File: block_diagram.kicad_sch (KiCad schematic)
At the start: 0 parts

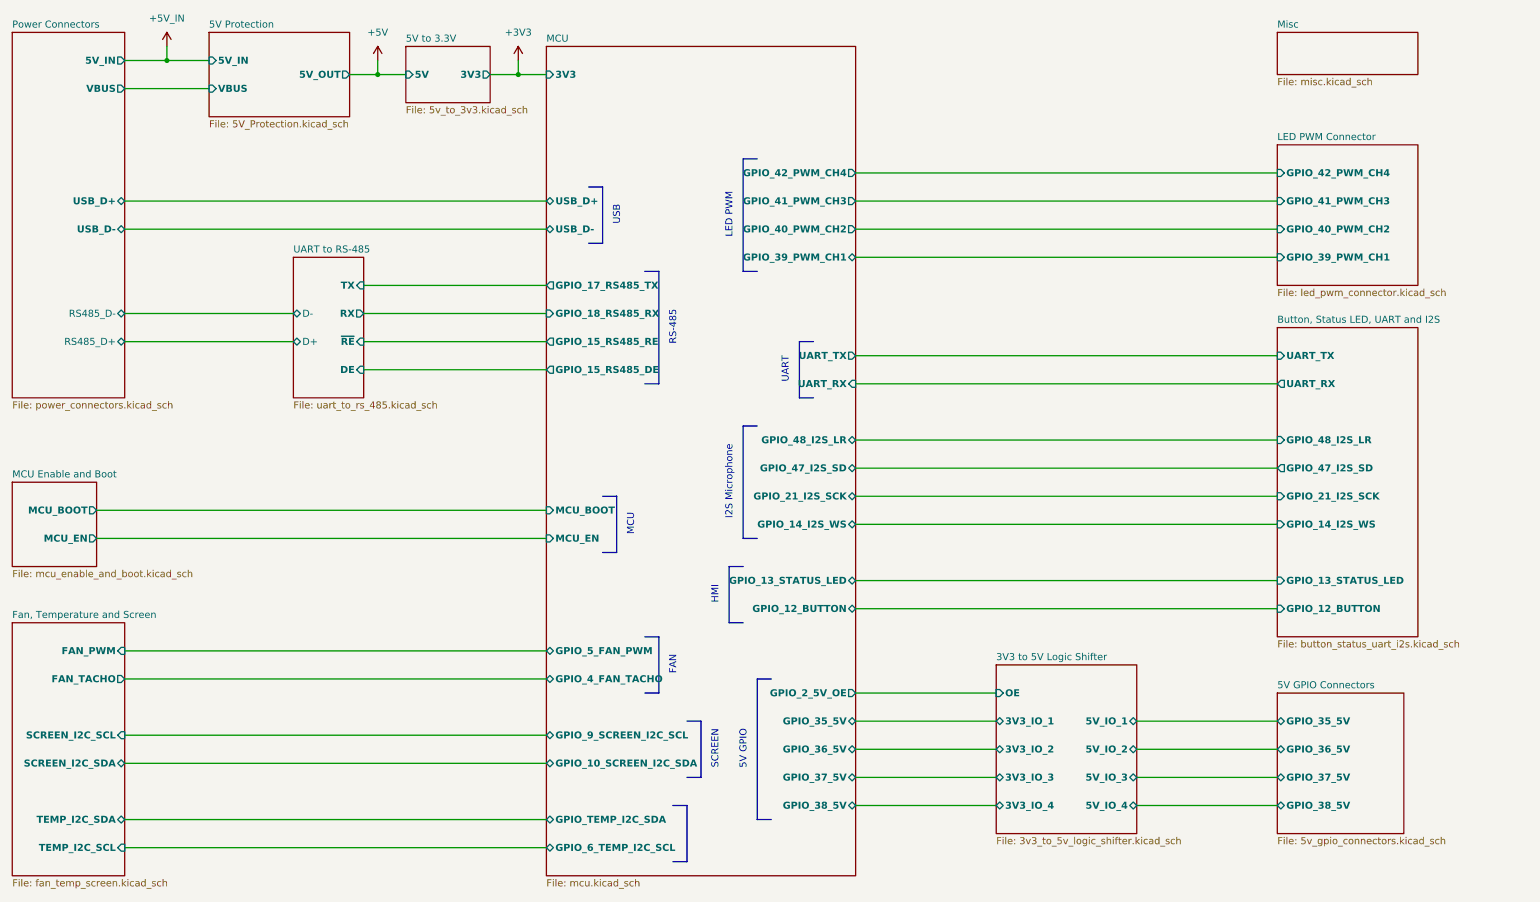
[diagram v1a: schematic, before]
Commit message: Finished layout no drc or erc errors
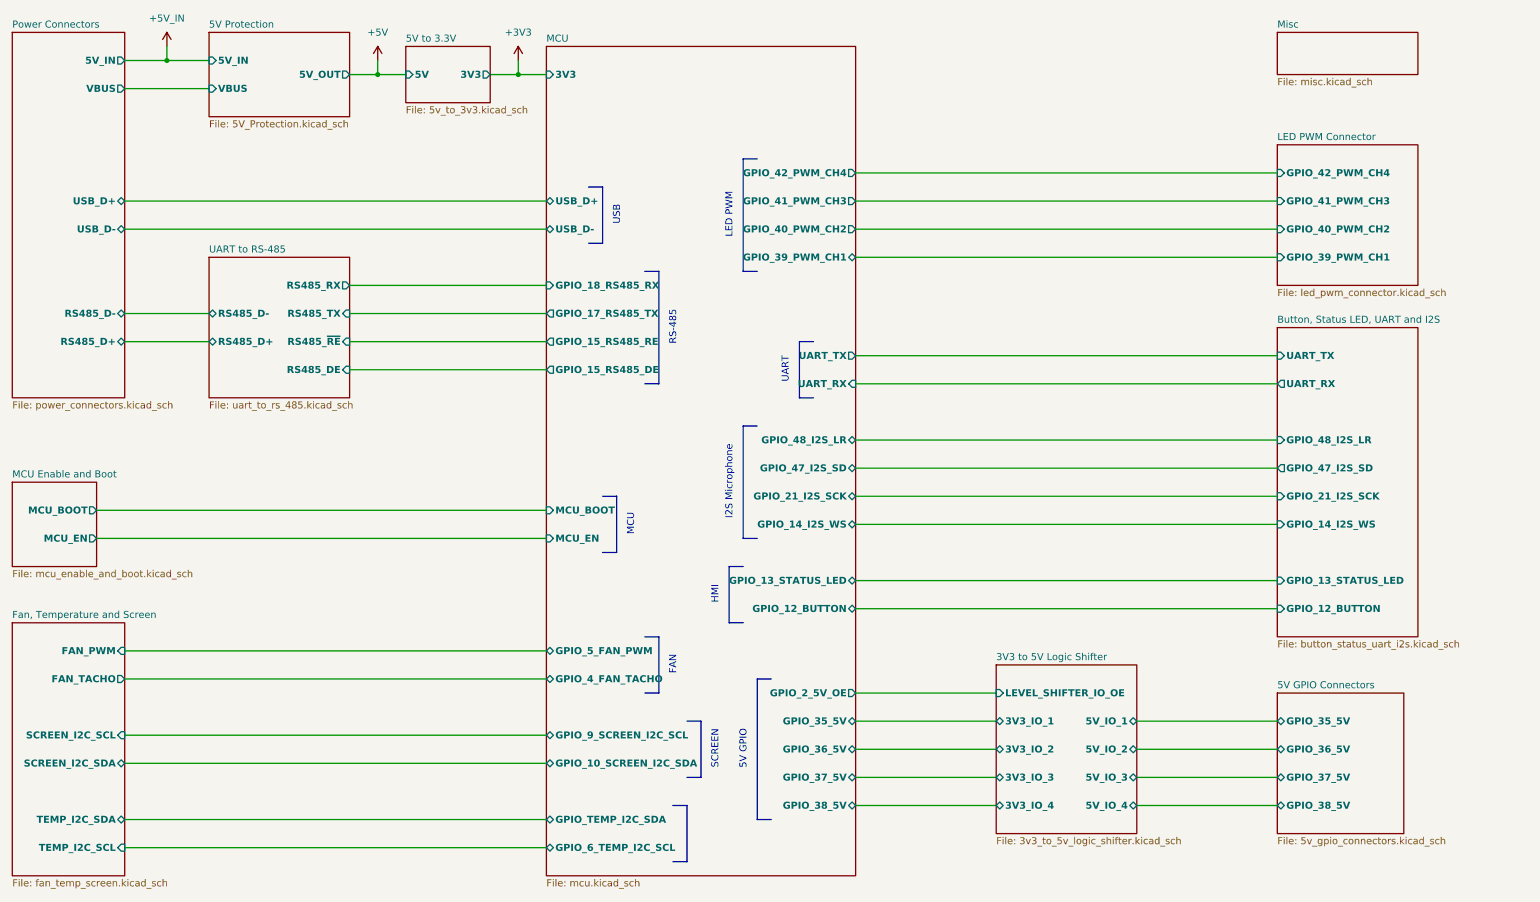
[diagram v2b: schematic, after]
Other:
- sheet 3V3 to 5V Logic Shifter ports: added LEVEL_SHIFTER_IO_OE; removed OE
- sheet UART to RS-485 ports: added RS485_D+, RS485_D-, RS485_DE, RS485_RX, RS485_TX, RS485_~{RE}; removed D+, D-, DE, RX, TX, ~{RE}
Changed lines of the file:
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@@
-	(wire
-		(pts
-			(xy 78.74 63.5) (xy 111.76 63.5)
-		)
-		(stroke
-			(width 0)
-			(type default)
-		)
-	)
 	(wire
 		(pts
@@
 		)
 	)
-	(wire
-		(pts
-			(xy 78.74 68.58) (xy 111.76 68.58)
-		)
-		(stroke
-			(width 0)
-			(type default)
-		)
-	)
 	(polyline
 		(pts
@@
 	(wire
 		(pts
+			(xy 76.2 78.74) (xy 111.76 78.74)
+		)
+		(stroke
+			(width 0)
+			(type default)
+		)
+	)
+	(wire
+		(pts
 			(xy 35.56 48.26) (xy 111.76 48.26)
 		)
@@
 		)
 	)
+	(wire
+		(pts
+			(xy 76.2 68.58) (xy 111.76 68.58)
+		)
+		(stroke
+			(width 0)
+			(type default)
+		)
+	)
 	(polyline
 		(pts
@@
 		)
 	)
+	(wire
+		(pts
+			(xy 76.2 63.5) (xy 111.76 63.5)
+		)
+		(stroke
+			(width 0)
+			(type default)
+		)
+	)
 	(polyline
 		(pts
@@
 		)
 	)
-	(wire
-		(pts
-			(xy 78.74 73.66) (xy 111.76 73.66)
-		)
-		(stroke
-			(width 0)
-			(type default)
-		)
-	)
 	(polyline
 		(pts
@@
 	(wire
 		(pts
-			(xy 35.56 68.58) (xy 66.04 68.58)
+			(xy 35.56 68.58) (xy 50.8 68.58)
 		)
 		(stroke
@@
 	(wire
 		(pts
-			(xy 35.56 73.66) (xy 66.04 73.66)
+			(xy 76.2 73.66) (xy 111.76 73.66)
+		)
+		(stroke
+			(width 0)
+			(type default)
+		)
+	)
+	(wire
+		(pts
+			(xy 35.56 73.66) (xy 50.8 73.66)
 		)
 		(stroke
@@
 		(pts
 			(xy 147.32 88.9) (xy 147.32 109.22)
-		)
-		(stroke
-			(width 0)
-			(type default)
-		)
-	)
-	(wire
-		(pts
-			(xy 78.74 78.74) (xy 111.76 78.74)
 		)
 		(stroke
@@
 			)
 		)
-		(pin "OE" input
-			(at 193.04 137.16 180)
-			(effects
-				(font
-					(size 1.27 1.27)
-					(thickness 0.254)
-					(bold yes)
-				)
-				(justify left)
-			)
-		)
 		(pin "3V3_IO_1" bidirectional
 			(at 193.04 142.24 180)
@@
 				)
 				(justify right)
+			)
+		)
+		(pin "LEVEL_SHIFTER_IO_OE" input
+			(at 193.04 137.16 180)
+			(effects
+				(font
+					(size 1.27 1.27)
+					(thickness 0.254)
+					(bold yes)
+				)
+				(justify left)
 			)
 		)
@@
 		)
 		(pin "GPIO_17_RS485_TX" output
+			(at 111.76 68.58 180)
+			(effects
+				(font
+					(size 1.27 1.27)
+					(thickness 0.254)
+					(bold yes)
+				)
+				(justify left)
+			)
+		)
+		(pin "GPIO_18_RS485_RX" input
 			(at 111.76 63.5 180)
-			(effects
-				(font
-					(size 1.27 1.27)
-					(thickness 0.254)
-					(bold yes)
-				)
-				(justify left)
-			)
-		)
-		(pin "GPIO_18_RS485_RX" input
-			(at 111.76 68.58 180)
 			(effects
 				(font
@@
 	)
 	(sheet
-		(at 66.04 58.42)
-		(size 12.7 25.4)
+		(at 50.8 58.42)
+		(size 25.4 25.4)
 		(fields_autoplaced yes)
 		(stroke
@@
 		)
 		(property "Sheetname" "UART to RS-485"
-			(at 66.04 57.7084 0)
+			(at 50.8 57.7084 0)
 			(effects
 				(font
@@
 		)
 		(property "Sheetfile" "uart_to_rs_485.kicad_sch"
-			(at 66.04 84.4046 0)
+			(at 50.8 84.4046 0)
 			(effects
 				(font
@@
 			)
 		)
-		(pin "DE" input
-			(at 78.74 78.74 0)
-			(effects
-				(font
-					(size 1.27 1.27)
-					(thickness 0.254)
-					(bold yes)
-				)
-				(justify right)
-			)
-		)
-		(pin "TX" input
-			(at 78.74 63.5 0)
-			(effects
-				(font
-					(size 1.27 1.27)
-					(thickness 0.254)
-					(bold yes)
-				)
-				(justify right)
-			)
-		)
-		(pin "RX" output
-			(at 78.74 68.58 0)
-			(effects
-				(font
-					(size 1.27 1.27)
-					(thickness 0.254)
-					(bold yes)
-				)
-				(justify right)
-			)
-		)
-		(pin "~{RE}" input
-			(at 78.74 73.66 0)
-			(effects
-				(font
-					(size 1.27 1.27)
-					(thickness 0.254)
-					(bold yes)
-				)
-				(justify right)
-			)
-		)
-		(pin "D-" bidirectional
-			(at 66.04 68.58 180)
-			(effects
-				(font
-					(size 1.27 1.27)
-				)
-				(justify left)
-			)
-		)
-		(pin "D+" bidirectional
-			(at 66.04 73.66 180)
-			(effects
-				(font
-					(size 1.27 1.27)
-				)
-				(justify left)
+		(pin "RS485_D-" bidirectional
+			(at 50.8 68.58 180)
+			(effects
+				(font
+					(size 1.27 1.27)
+					(thickness 0.254)
+					(bold yes)
+				)
+				(justify left)
+			)
+		)
+		(pin "RS485_D+" bidirectional
+			(at 50.8 73.66 180)
+			(effects
+				(font
+					(size 1.27 1.27)
+					(thickness 0.254)
+					(bold yes)
+				)
+				(justify left)
+			)
+		)
+		(pin "RS485_DE" input
+			(at 76.2 78.74 0)
+			(effects
+				(font
+					(size 1.27 1.27)
+					(thickness 0.254)
+					(bold yes)
+				)
+				(justify right)
+			)
+		)
+		(pin "RS485_RX" output
+			(at 76.2 63.5 0)
+			(effects
+				(font
+					(size 1.27 1.27)
+					(thickness 0.254)
+					(bold yes)
+				)
+				(justify right)
+			)
+		)
+		(pin "RS485_~{RE}" input
+			(at 76.2 73.66 0)
+			(effects
+				(font
+					(size 1.27 1.27)
+					(thickness 0.254)
+					(bold yes)
+				)
+				(justify right)
+			)
+		)
+		(pin "RS485_TX" input
+			(at 76.2 68.58 0)
+			(effects
+				(font
+					(size 1.27 1.27)
+					(thickness 0.254)
+					(bold yes)
+				)
+				(justify right)
 			)
 		)
@@
 				(font
 					(size 1.27 1.27)
+					(thickness 0.254)
+					(bold yes)
 				)
 				(justify right)
@@
 				(font
 					(size 1.27 1.27)
-				)
-				(justify right)
+					(thickness 0.254)
+					(bold yes)
+				)
+				(justify right)

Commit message: Ready for kibot
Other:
- sheet Button, Status LED, UART and I2S ports: added BUTTON, I2S_LR, I2S_SCK, I2S_SD, I2S_WS, STATUS_LED; removed GPIO_12_BUTTON, GPIO_13_STATUS_LED, GPIO_14_I2S_WS, GPIO_21_I2S_SCK, GPIO_47_I2S_SD, GPIO_48_I2S_LR
- sheet LED PWM Connector ports: added PWM_CH1, PWM_CH2, PWM_CH3, PWM_CH4; removed GPIO_39_PWM_CH1, GPIO_40_PWM_CH2, GPIO_41_PWM_CH3, GPIO_42_PWM_CH4
- sheet MCU ports: added GPIO_12_STATUS_LED, GPIO_13_BUTTON, GPIO_14_I2S_LR, GPIO_15_PWM_CH4, GPIO_16_PWM_CH3, GPIO_17_PWM_CH2, GPIO_18_PWM_CH1, GPIO_1_5V_OE, GPIO_21_I2S_WS, GPIO_35_FAN_PWM, GPIO_36_FAN_TACHO, GPIO_37_TEMP_I2C_SCL, GPIO_38_TEMP_I2C_SDA, GPIO_39_5V, GPIO_40_5V, GPIO_41_5V, GPIO_42_5V, GPIO_47_I2S_SCK, GPIO_48_I2S_SD, GPIO_4_RS485_TX, GPIO_5_RS485_DE, GPIO_6_RS485_RE, GPIO_7_RS485_RX; removed GPIO_12_BUTTON, GPIO_13_STATUS_LED, GPIO_14_I2S_WS, GPIO_15_RS485_DE, GPIO_15_RS485_RE, GPIO_17_RS485_TX, GPIO_18_RS485_RX, GPIO_21_I2S_SCK, GPIO_2_5V_OE, GPIO_35_5V, GPIO_36_5V, GPIO_37_5V, GPIO_38_5V, GPIO_39_PWM_CH1, GPIO_40_PWM_CH2, GPIO_41_PWM_CH3, GPIO_42_PWM_CH4, GPIO_47_I2S_SD, GPIO_48_I2S_LR, GPIO_4_FAN_TACHO, GPIO_5_FAN_PWM, GPIO_6_TEMP_I2C_SCL, GPIO_TEMP_I2C_SDA

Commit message: workflow
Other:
- title: (none) -> Block Diagram
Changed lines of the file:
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@@
 	(generator_version "8.0")
 	(paper "A4")
+	(title_block
+		(title "Block Diagram")
+	)
 	(junction
 		(at 106.68 25.4)
@@
 			(project "AstraControl"
 				(path "/9a751838-dce8-4d69-8a02-736625ac74e7/0db21d8e-3390-4d67-877f-0e5d98e37848"
-					(page "13")
+					(page "11")
 				)
 			)
@@
 			(project "AstraControl"
 				(path "/9a751838-dce8-4d69-8a02-736625ac74e7/0db21d8e-3390-4d67-877f-0e5d98e37848"
-					(page "8")
+					(page "7")
 				)
 			)
@@
 			(project "AstraControl"
 				(path "/9a751838-dce8-4d69-8a02-736625ac74e7/0db21d8e-3390-4d67-877f-0e5d98e37848"
-					(page "5")
+					(page "4")
 				)
 			)
@@
 			(project "AstraControl"
 				(path "/9a751838-dce8-4d69-8a02-736625ac74e7/0db21d8e-3390-4d67-877f-0e5d98e37848"
-					(page "16")
+					(page "15")
 				)
 			)
@@
 			(project "AstraControl"
 				(path "/9a751838-dce8-4d69-8a02-736625ac74e7/0db21d8e-3390-4d67-877f-0e5d98e37848"
-					(page "11")
+					(page "10")
 				)
 			)
@@
 			(project "AstraControl"
 				(path "/9a751838-dce8-4d69-8a02-736625ac74e7/0db21d8e-3390-4d67-877f-0e5d98e37848"
-					(page "14")
+					(page "13")
 				)
 			)
@@
 			(project "AstraControl"
 				(path "/9a751838-dce8-4d69-8a02-736625ac74e7/0db21d8e-3390-4d67-877f-0e5d98e37848"
-					(page "6")
+					(page "5")
 				)
 			)
@@
 			(project "AstraControl"
 				(path "/9a751838-dce8-4d69-8a02-736625ac74e7/0db21d8e-3390-4d67-877f-0e5d98e37848"
-					(page "9")
+					(page "8")
 				)
 			)
@@
 			(project "AstraControl"
 				(path "/9a751838-dce8-4d69-8a02-736625ac74e7/0db21d8e-3390-4d67-877f-0e5d98e37848"
-					(page "7")
+					(page "6")
 				)
 			)
@@
 			(project "AstraControl"
 				(path "/9a751838-dce8-4d69-8a02-736625ac74e7/0db21d8e-3390-4d67-877f-0e5d98e37848"
-					(page "16")
+					(page "14")
 				)
 			)
@@
 			(project "AstraControl"
 				(path "/9a751838-dce8-4d69-8a02-736625ac74e7/0db21d8e-3390-4d67-877f-0e5d98e37848"
-					(page "20")
-				)
-			)
+					(page "16")
+				)
+			)
